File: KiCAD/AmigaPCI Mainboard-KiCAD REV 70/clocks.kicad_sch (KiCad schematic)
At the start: 37 parts, among them CN201 USB_A_Stacked, U108 74AHC04, U210 AT27C4096, U211 AT27C4096, U219 74AHC04, U223 SST39VF1601C, U225 USBLC6-2SC6, U226 USBLC6-2SC6, U228 AP2156SG-13, U815 74LVC08, X2 33MHz, X3 28.63636MHz

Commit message: Add JLCPCB part numbers and fix 74LVC244 footprints.
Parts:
- C135, C214, C215, C229, C238, C239, C246, C253, C259, C262, C821: LCSC (none) -> C14663
- C216, C217: LCSC (none) -> C439891
- CN201: LCSC (none) -> C5366339
- R140, R141, R142, R143, R144, R145, R216: LCSC (none) -> C23345
- R230, R231, R232, R233: LCSC (none) -> C23182
- R265: LCSC (none) -> C25804
- U108, U219: LCSC (none) -> C8190
- U210, U211: LCSC (none) -> C2332
- U223: LCSC (none) -> C184156
- U225, U226: LCSC (none) -> C7519
- U228: LCSC (none) -> C88233
- U815: LCSC (none) -> C6053
- X2: LCSC (none) -> C17506154
- X3: LCSC (none) -> C1670933

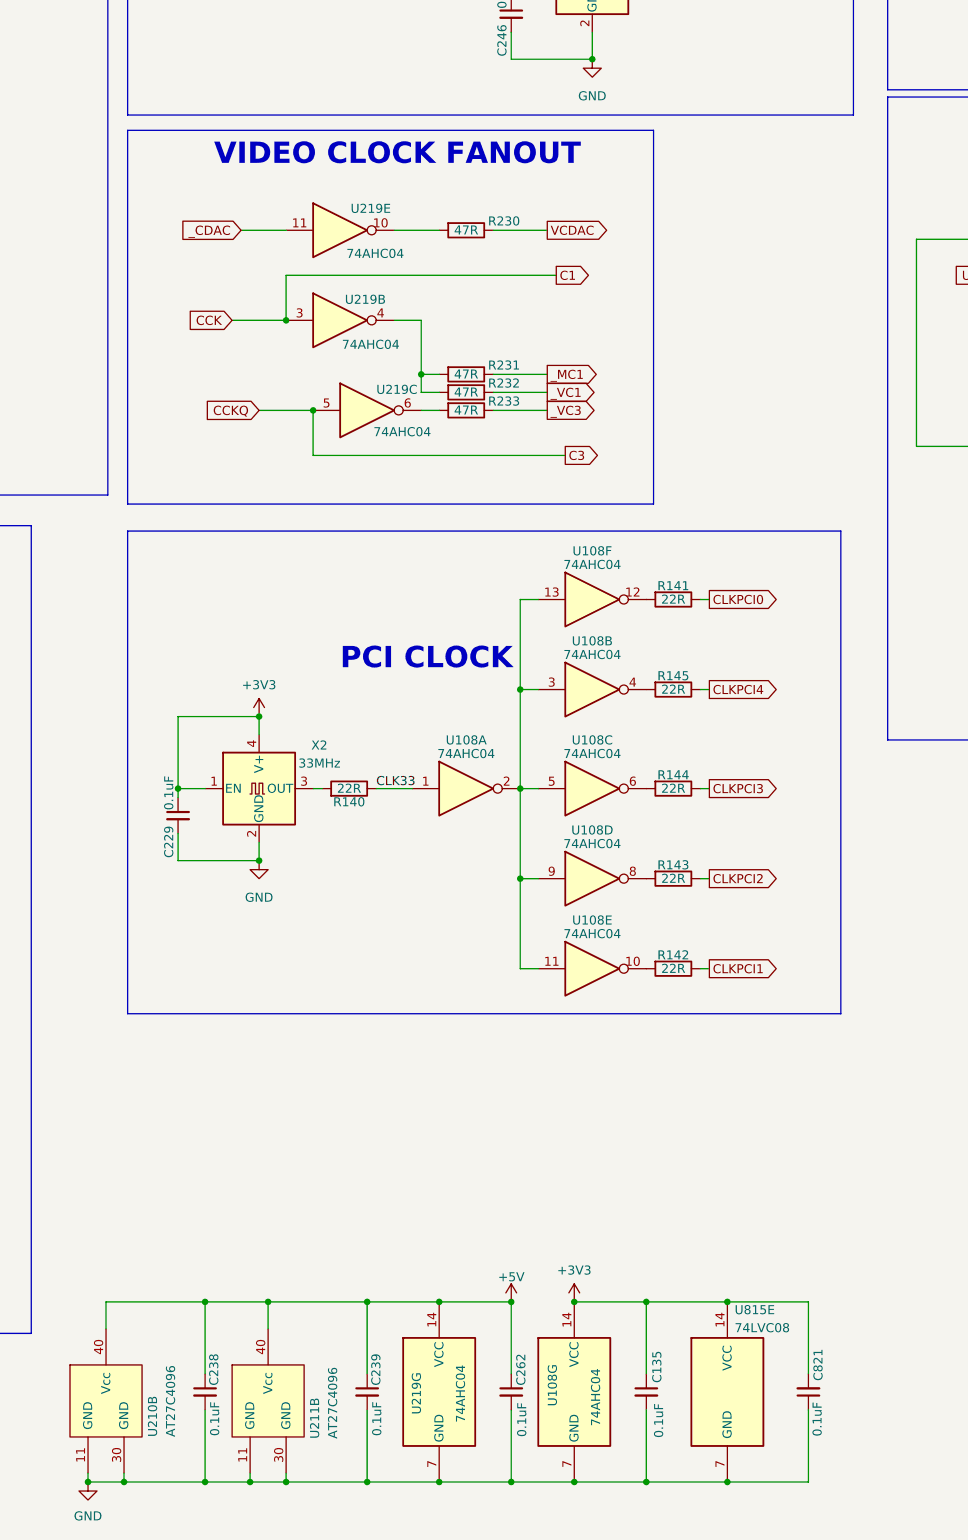
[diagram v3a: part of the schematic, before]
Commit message: Updates to revision 7 board.
Change U810 to 74LVC245 buffers
Add CDAC to U712
Add address latch to CIAs
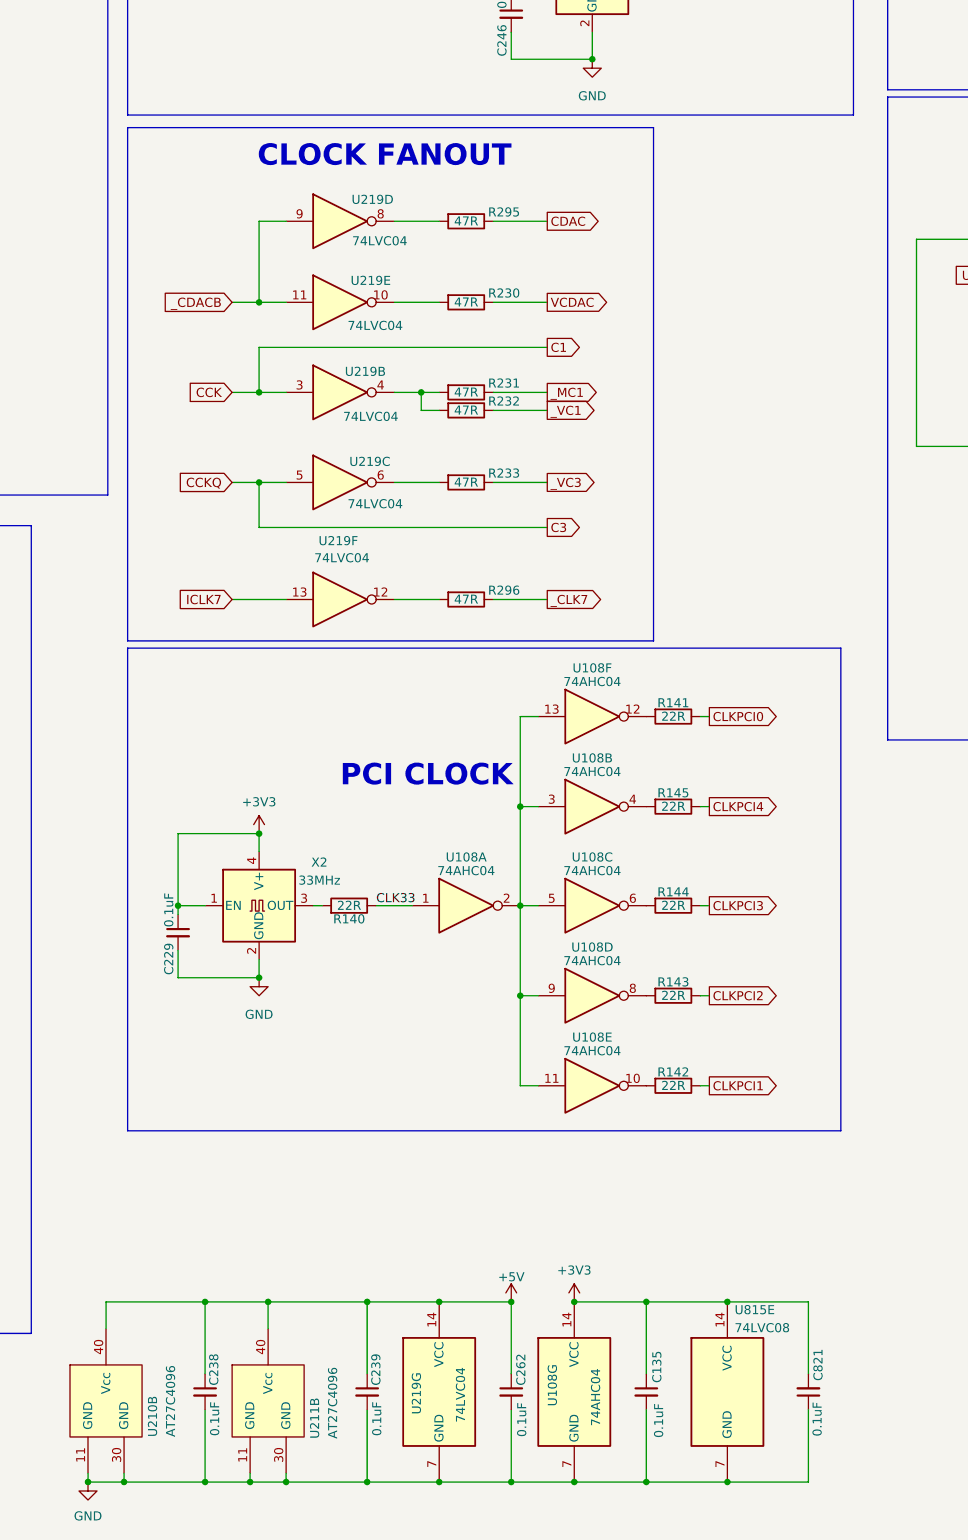
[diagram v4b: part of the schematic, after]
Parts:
- added R295, R296: 47R, Resistor_SMD:R_0603_1608Metric, symbol Device:R
- added unit 4 of U219
- added unit 6 of U219
- U219: value 74AHC04 -> 74LVC04; LCSC C8190 -> C352968
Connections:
- net _CDAC renamed _CDACB
- net _CDACB: now also U219.9
- new net: R295.2, U219.8
- new net: R296.2, U219.12
- new net CDAC: R295.1
- new net ICLK7: U219.13
- new net _CLK7: R296.1
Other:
- note added: "CLOCK FANOUT"
- note removed: "VIDEO CLOCK FANOUT"
- moved on the sheet: C229, R140, R141, R142, R143, R144, R145, R230, R231, R232, R233, U108A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

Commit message: New hardware rev files.
Gerber
BOM w/JLCPCB part numbers
Pick-n-Place File
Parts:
- U219: LCSC C352968 -> C352968
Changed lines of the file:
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@@
 			)
 		)
-		(property "LCSC" " C352968"
+		(property "LCSC" "C352968"
 			(at 175.26 80.01 0)
 			(effects
@@
 			)
 		)
-		(property "LCSC" " C352968"
+		(property "LCSC" "C352968"
 			(at 175.26 133.35 0)
 			(effects
@@
 			)
 		)
-		(property "LCSC" " C352968"
+		(property "LCSC" "C352968"
 			(at 189.23 245.11 0)
 			(effects
@@
 			)
 		)
-		(property "LCSC" " C352968"
+		(property "LCSC" "C352968"
 			(at 175.26 116.84 0)
 			(effects
@@
 			)
 		)
-		(property "LCSC" " C352968"
+		(property "LCSC" "C352968"
 			(at 175.26 104.14 0)
 			(effects
@@
 			)
 		)
-		(property "LCSC" " C352968"
+		(property "LCSC" "C352968"
 			(at 175.26 91.44 0)
 			(effects
